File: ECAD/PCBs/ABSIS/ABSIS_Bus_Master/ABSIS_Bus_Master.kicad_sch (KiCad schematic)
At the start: 40 parts, among them J1 Mini-Fit Jr. 2x04, J2 Mini-Fit Jr. 2x03, J3 Mini-Fit Jr. 2x03, J4 Mini-Fit Jr. 2x03, J5 PinHeader_2x11, P1 Power, P2 Analog, P3 Analog, P4 Digital, P5 PWM, P6 PWM, P7 Communication, U1 MAX487EESA+T, U2 MAX487EESA+T, U3 MAX487EESA+T

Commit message: General ECAD cleanup
Moved original OH design to legacy folder
Moved externally provided library symbols, footprints, and STEP files to appropriate OH library locations.
Upgraded project to KiCAD 10
Removed production files from ABSIS Pro_Micro since it is not yet production ready.
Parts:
- removed C1, C2, C3: 0.1uF, OH_Footprints:C_0805_2012Metric, symbol OH_Symbols:Capacitor_0805_0.1uF
- removed TP10: TP-B3A, TestPoint:TestPoint_THTPad_D1.5mm_Drill0.7mm, symbol Connector:TestPoint_Alt
- removed TP5: TP-B1B, TestPoint:TestPoint_THTPad_D1.5mm_Drill0.7mm, symbol Connector:TestPoint_Alt
- removed TP6: TP-B1A, TestPoint:TestPoint_THTPad_D1.5mm_Drill0.7mm, symbol Connector:TestPoint_Alt
- removed TP7: TP-B2B, TestPoint:TestPoint_THTPad_D1.5mm_Drill0.7mm, symbol Connector:TestPoint_Alt
- removed TP8: TP-B2A, TestPoint:TestPoint_THTPad_D1.5mm_Drill0.7mm, symbol Connector:TestPoint_Alt
- removed TP9: TP-B3B, TestPoint:TestPoint_THTPad_D1.5mm_Drill0.7mm, symbol Connector:TestPoint_Alt
- removed U1, U2, U3: MAX487EESA+T, OH_Footprints:SOIC-8_3.9x4.9mm_P1.27mm, symbol OH_Symbols:Controller_MAX487E
- added C1, C2, C3: 0.1uF, Capacitor_SMD:C_0805_2012Metric, symbol Device:C
- added D1, D2, D3: CDSOT23-SM712, CDSOT23-SM712:CDSOT23-SM712, symbol CDSOT23-SM712:CDSOT23-SM712
- added D4: SS54, SS54:SS54, symbol SS54:SS54
- added IC1, IC2, IC3: THVD1410DR, THVD1410DR:THVD1410DR, symbol THVD1410DR:THVD1410DR
- added J6: Screw_Terminal_01x01, TerminalBlock_Wuerth:Wuerth_REDCUBE-THR_WP-THRBU_74650073_THR, symbol Connector:Screw_Terminal_01x01
- added R10, R13, R14, R4, R5, R9: 10Ω, Resistor_SMD:R_0805_2012Metric, symbol Device:R
- added R11, R15, R6: 120Ω, Resistor_SMD:R_0805_2012Metric, symbol Device:R
- added R12, R7, R8: 10kΩ, Resistor_SMD:R_0805_2012Metric, symbol Device:R
- added TP11, TP13, TP15: TP-B1B, TestPoint:TestPoint_THTPad_D1.5mm_Drill0.7mm, symbol Connector:TestPoint_Alt
- added TP12, TP14, TP16: TP-B1A, TestPoint:TestPoint_THTPad_D1.5mm_Drill0.7mm, symbol Connector:TestPoint_Alt
- R1, R2, R3: value 120 -> 10kΩ; footprint Resistor_SMD:R_0805_2012Metric_Pad1.15x1.40mm_HandSolder -> Resistor_SMD:R_0805_2012Metric; LCSC C17437 -> C140868; Manufacturer PN (none) -> AC0805FR-0710KL
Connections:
- net +12V_SUPPLY: now also D4.1 (A); no longer P1.8 (Pin_8)
- net +5V: now also C1.2, C2.2, C3.2, IC1.8 (VCC), IC2.6 (A), IC2.8 (VCC), IC3.8 (VCC), R10.1, R12.1, R7.1, R8.1
- net 14(Tx3): now also IC3.4 (D)
- net 15(Rx3): now also IC3.1 (R), R12.2
- net 16(Tx2): now also IC2.4 (D)
- net 17(Rx2): now also IC2.1 (R), R8.2
- net 18(Tx1): now also IC1.4 (D)
- net 19(Rx1): now also IC1.1 (R), R7.2
- net 2(**): now also R1.1, IC1.2 (~{RE}), IC1.3 (DE)
- net 3(**): now also R2.1, IC2.2 (~{RE}), IC2.3 (DE)
- net 4(**): now also R3.1, IC3.2 (~{RE}), IC3.3 (DE)
- net BUS1-A: now also D2.1, R5.2, R6.2, TP12.1; no longer R1.2
- net BUS1-B: now also D2.2, R4.2, R6.1, TP11.1; no longer R1.1
- net BUS2-A: now also D1.1, R10.2, R11.2, TP14.1; no longer R2.2
- net BUS2-B: now also D1.2, R11.1, R9.2, TP13.1; no longer R2.1
- net BUS3-A: now also D3.1, R14.2, R15.2, TP16.1; no longer R3.2
- net BUS3-B: now also D3.2, R13.2, R15.1, TP15.1; no longer R3.1
- net GND: now also R1.2, R2.2, R3.2, C1.1, C2.1, C3.1, D1.3, D2.3, D3.3, IC1.5 (GND), IC2.5 (GND), IC3.5 (GND), J6.1 (Pin_1)
- new net: D4.2 (K), P1.8 (Pin_8)
- new net: IC1.6 (A), R5.1
- new net: IC1.7 (B), R4.1
- new net: IC2.7 (B), R9.1
- new net: IC3.7 (B), R13.1
- new net: IC3.6 (A), R14.1
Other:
- note added: "1) J5 / IO CONNECTORS MAY NOT FUNCTION WITH DCS-BIOS WHILE MASTER FUNCTIONALITY IS IN USE. 2) ABSIS RS485 BUS SPECIFICATION 2.1) BUS IS HALF DUPLEX: EITHER TRANSMITTING OR RECIEVING AT ANY GIVEN TIME. 2.2) PIN FUNCTION: R: DATA OUTPUT / D: DATA INPUT / DE HAS INTERNAL PULL-DOWN (DRIVER DISABLED BY DEFAULT) / RE HAS INTERNAL PULL-UP (RECIEVER DISABLED BY DEFAULT) 2.3) CIRCUIT CONTAINS OPEN, SHORT,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"
- note added: "ACTIVE HIGH"
- note added: "ACTIVE LOW"
- note added: "TODO: MOVE SYMBOLS TO OH LIBRARIES POINT AFFECTED SYMBOLS/FOOTPRINTS/STEP AT OH LIBRARIES PCB: ROTATE MOLEX CONNECTOR TO MINIMIZE RS485 STUB LENGTH ADD 2 VIAs EACH TO VCC AND GND ON THE TRANSCEIVER CHECK SILKSCREEN, ADJUST AS REQUIRED"
- note removed: "1) J5 / IO CONNECTORS MAY NOT FUNCTION WITH DCS-BIOS WHILE MASTER FUNCTIONALITY IS IN USE."
- moved on the sheet: J1, J2, J3, J4, J5, MK1, MK3, MK4, MK6, P1, P2, P3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

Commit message: Schematic: changed symbols to OH libs
Changed the new symbols to the OH lib versions.
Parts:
- D1, D2, D3: footprint CDSOT23-SM712:CDSOT23-SM712 -> OH_Footprints:CDSOT23-SM712; symbol CDSOT23-SM712:CDSOT23-SM712 -> OH Symbols:CDSOT23-SM712; Arrow Part Number (none) -> CDSOT23-SM712; Arrow Price/Stock (none) -> https://www.arrow.com/en/products/cdsot23-sm712/bourns?utm_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; Height (none) -> 1.17; Manufacturer_Name (none) -> Bourns; Manufacturer_Part_Number (none) -> CDSOT23-SM712; Mouser Part Number (none) -> 652-CDSOT23-SM712; Mouser Price/Stock (none) -> https://www.mouser.co.uk/ProductDetail/Bourns/CDSOT23-SM712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
- D4: footprint SS54:SS54 -> OH_Footprints:SS54; symbol SS54:SS54 -> OH Symbols:SS54; Height (none) -> 2.62; Manufacturer_Name (none) -> MDD; Manufacturer_Part_Number (none) -> SS54
- IC1, IC2, IC3: footprint THVD1410DR:THVD1410DR -> OH_Footprints:THVD1410DR; symbol THVD1410DR:THVD1410DR -> OH Symbols:THVD1410DR; Arrow Part Number (none) -> THVD1410DR; Arrow Price/Stock (none) -> https://www.arrow.com/en/products/thvd1410dr/texas-instrume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; Height (none) -> 1.75; Manufacturer_Name (none) -> Texas Instruments; Manufacturer_Part_Number (none) -> THVD1410DR; Mouser Part Number (none) -> 595-THVD1410DR; Mouser Price/Stock (none) -> https://www.mouser.co.uk/ProductDetail/Texas-Instruments/TH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
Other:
- moved on the sheet: C3, D3, IC3, R12, R13, R14, R15, R3, TP15, TP16

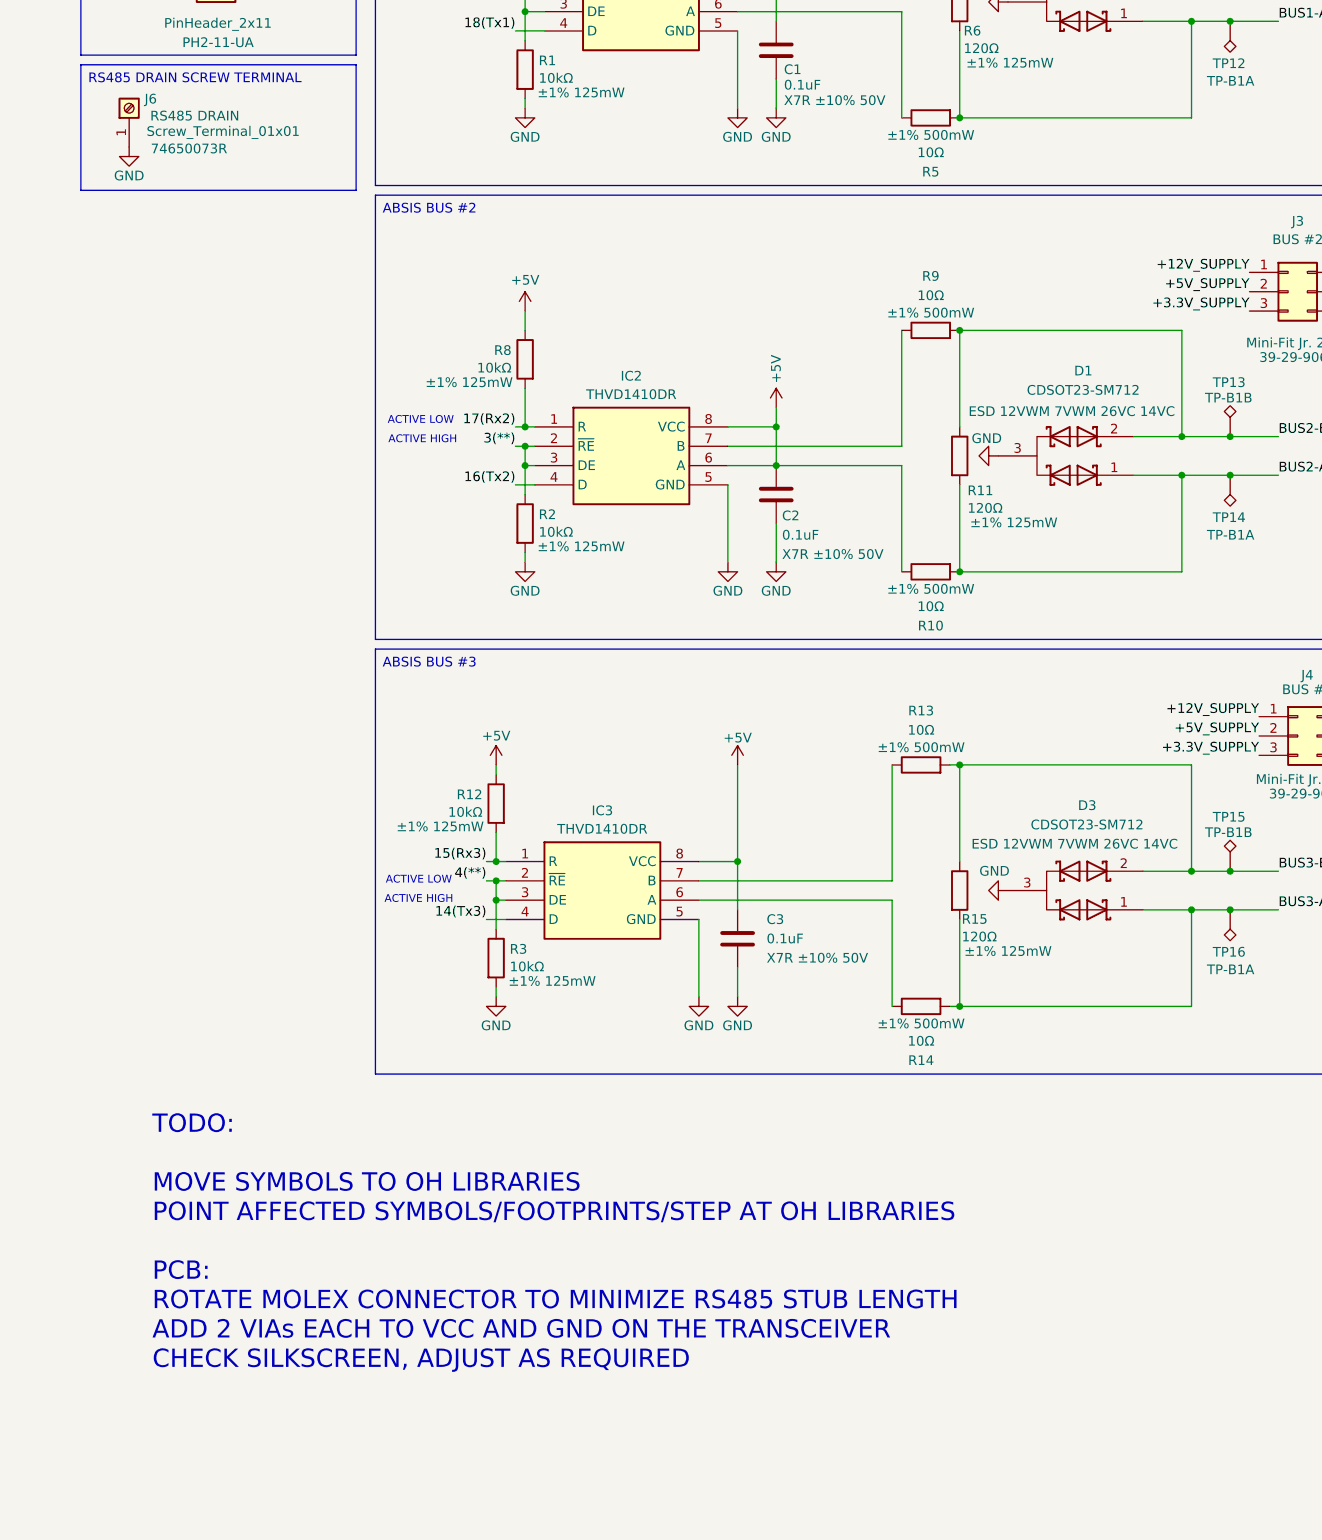
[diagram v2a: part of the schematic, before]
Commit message: PCB Updates
Made all components display 3D models
Updated silkscreens
Added RS485 Drain Screw Terminal to PCB
Also add new 3D model file ECAD/lib/OH_3DModels/360272.stp.
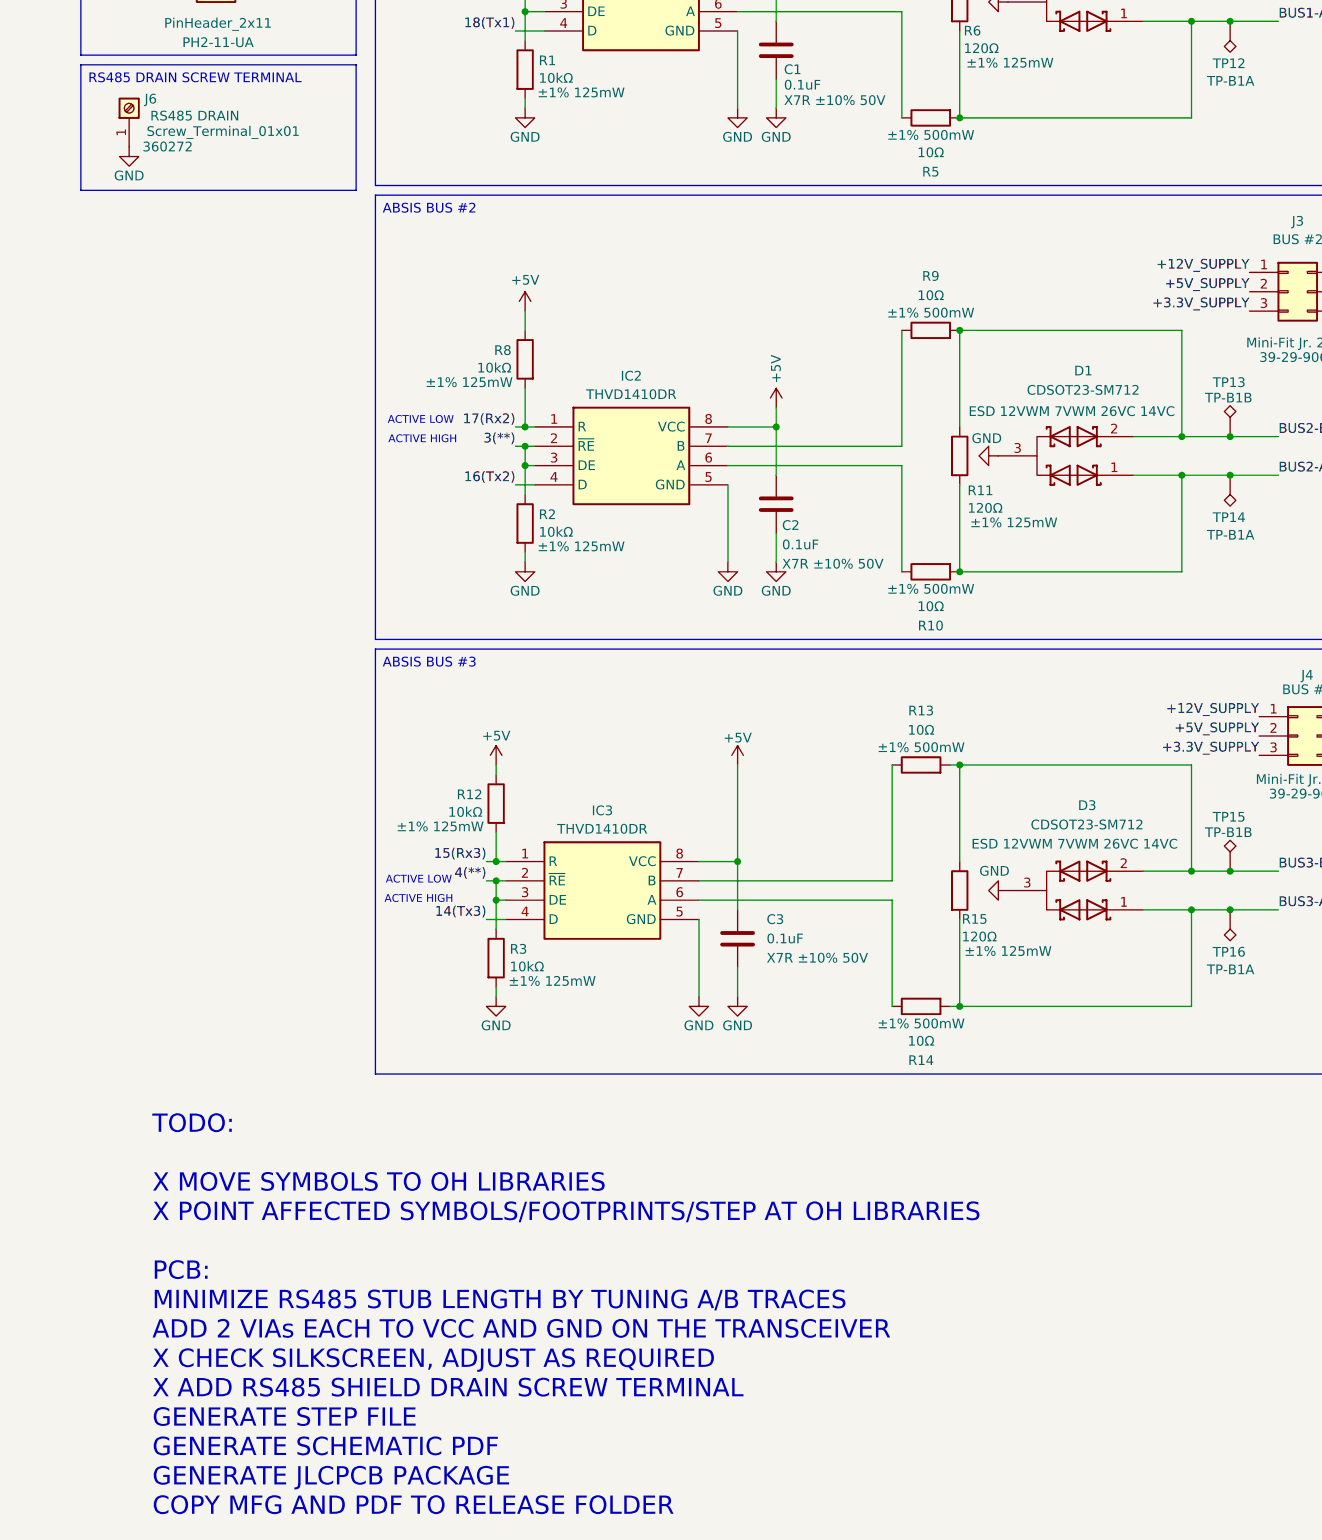
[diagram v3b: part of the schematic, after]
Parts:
- J6: footprint TerminalBlock_Wuerth:Wuerth_REDCUBE-THR_WP-THRBU_74650073_THR -> TerminalBlock_MetzConnect:TerminalBlock_MetzConnect_360272_1x01_Horizontal_ScrewM2.6; Manufacturer PN 74650073R -> 360272
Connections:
- net +5V: no longer IC2.6 (A), R10.1
- new net: IC2.6 (A), R10.1
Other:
- note added: "TODO: X MOVE SYMBOLS TO OH LIBRARIES X POINT AFFECTED SYMBOLS/FOOTPRINTS/STEP AT OH LIBRARIES PCB: MINIMIZE RS485 STUB LENGTH BY TUNING A/B TRACES ADD 2 VIAs EACH TO VCC AND GND ON THE TRANSCEIVER X CHECK SILKSCREEN, ADJUST AS REQUIRED X ADD RS485 SHIELD DRAIN SCREW TERMINAL GENERATE STEP FILE GENERATE SCHEMATIC PDF GENERATE JLCPCB PACKAGE COPY MFG AND PDF TO RELEASE FOLDER"
- note removed: "TODO: MOVE SYMBOLS TO OH LIBRARIES POINT AFFECTED SYMBOLS/FOOTPRINTS/STEP AT OH LIBRARIES PCB: ROTATE MOLEX CONNECTOR TO MINIMIZE RS485 STUB LENGTH ADD 2 VIAs EACH TO VCC AND GND ON THE TRANSCEIVER CHECK SILKSCREEN, ADJUST AS REQUIRED"
- moved on the sheet: C2
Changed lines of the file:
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@@
 		)
 	)
-	(text "TODO:\n\nMOVE SYMBOLS TO OH LIBRARIES\nPOINT AFFECTED SYMBOLS/FOOTPRINTS/STEP AT OH LIBRARIES\n\nPCB:\nROTATE MOLEX CONNECTOR TO MINIMIZE RS485 STUB LENGTH\nADD 2 VIAs EACH TO VCC AND GND ON THE TRANSCEIVER\nCHECK SILKSCREEN, ADJUST AS REQUIRED"
+	(text "TODO:\n\nX MOVE SYMBOLS TO OH LIBRARIES\nX POINT AFFECTED SYMBOLS/FOOTPRINTS/STEP AT OH LIBRARIES\n\nPCB:\nMINIMIZE RS485 STUB LENGTH BY TUNING A/B TRACES\nADD 2 VIAs EACH TO VCC AND GND ON THE TRANSCEIVER\nX CHECK SILKSCREEN, ADJUST AS REQUIRED\nX ADD RS485 SHIELD DRAIN SCREW TERMINAL\nGENERATE STEP FILE\nGENERATE SCHEMATIC PDF\nGENERATE JLCPCB PACKAGE\nCOPY MFG AND PDF TO RELEASE FOLDER"
 		(exclude_from_sim no)
 		(at 147.828 193.294 0)
@@
 	)
 	(junction
-		(at 229.87 107.95)
-		(diameter 0)
-		(color 0 0 0 0)
-	)
-	(junction
 		(at 254 179.07)
 		(diameter 0)
@@
 	(wire
 		(pts
-			(xy 229.87 107.95) (xy 246.38 107.95)
+			(xy 223.52 107.95) (xy 246.38 107.95)
 		)
 		(stroke
@@
 	(wire
 		(pts
-			(xy 229.87 115.57) (xy 229.87 120.65)
+			(xy 229.87 116.84) (xy 229.87 120.65)
 		)
 		(stroke
@@
 	(wire
 		(pts
+			(xy 229.87 102.87) (xy 229.87 109.22)
+		)
+		(stroke
+			(width 0)
+			(type default)
+		)
+	)
+	(wire
+		(pts
 			(xy 354.33 113.03) (xy 354.33 110.49)
 		)
@@
 	(wire
 		(pts
-			(xy 229.87 102.87) (xy 229.87 107.95)
-		)
-		(stroke
-			(width 0)
-			(type default)
-		)
-	)
-	(wire
-		(pts
 			(xy 223.52 105.41) (xy 246.38 105.41)
 		)
@@
 	(wire
 		(pts
-			(xy 223.52 107.95) (xy 229.87 107.95)
-		)
-		(stroke
-			(width 0)
-			(type default)
-		)
-	)
-	(wire
-		(pts
 			(xy 378.46 111.76) (xy 378.46 113.03)
 		)
@@
 	(symbol
 		(lib_id "Device:C")
-		(at 229.87 111.76 180)
+		(at 229.87 113.03 180)
 		(unit 1)
 		(body_style 1)
@@
 		(dnp no)
 		(property "Reference" "C2"
-			(at 230.632 114.554 0)
+			(at 230.632 115.824 0)
 			(show_name no)
 			(do_not_autoplace no)
@@
 		)
 		(property "Value" "0.1uF"
-			(at 230.632 117.094 0)
+			(at 230.632 118.364 0)
 			(show_name no)
 			(do_not_autoplace no)
@@
 		)
 		(property "Footprint" "Capacitor_SMD:C_0805_2012Metric"
-			(at 228.9048 107.95 0)
+			(at 228.9048 109.22 0)
 			(hide yes)
 			(show_name no)
@@
 		)
 		(property "Datasheet" "https://datasheet.lcsc.com/szlcsc/YAGEO-CChttps://datasheet.lcsc.com/szlcsc/YAGEO-https://datasheet.lcsc.com/szlcsc/YAGEO-CC0805KRX7R9BB104_C49678.pdf"
-			(at 229.87 111.76 0)
+			(at 229.87 113.03 0)
 			(hide yes)
 			(show_name no)
@@
 		)
 		(property "Description" "X7R ±10% 50V"
-			(at 230.632 119.634 0)
+			(at 230.632 120.904 0)
 			(show_name no)
 			(do_not_autoplace no)
@@
 		)
 		(property "Manufacturer PN" "CC0805KRX7R9BB104"
-			(at 229.87 111.76 0)
+			(at 229.87 113.03 0)
 			(hide yes)
 			(show_name no)
@@
 		)
 		(property "LCSC" "C49678"
-			(at 229.87 111.76 0)
+			(at 229.87 113.03 0)
 			(hide yes)
 			(show_name no)
@@
 			)
 		)
-		(property "Footprint" "TerminalBlock_Wuerth:Wuerth_REDCUBE-THR_WP-THRBU_74650073_THR"
+		(property "Footprint" "TerminalBlock_MetzConnect:TerminalBlock_MetzConnect_360272_1x01_Horizontal_ScrewM2.6"
 			(at 144.78 60.96 0)
 			(hide yes)
@@
 			)
 		)
-		(property "Datasheet" "https://www.we-online.com/components/products/datasheet/74650073R.pdf"
+		(property "Datasheet" "https://www.metz-connect.com/externalfiles/360272/863849.PDF"
 			(at 144.78 60.96 0)
 			(hide yes)
@@
 			)
 		)
-		(property "Description" "M3 screw terminal"
+		(property "Description" "TERM BLOCK 1POS SIDE ENTRY"
 			(at 144.78 60.96 0)
 			(hide yes)
@@
 			)
 		)
-		(property "Manufacturer PN" "74650073R"
-			(at 152.654 66.294 90)
+		(property "Manufacturer PN" "  360272"
+			(at 149.86 66.04 90)
 			(show_name no)
 			(do_not_autoplace no)
